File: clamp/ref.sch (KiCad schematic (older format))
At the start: 11 parts, among them P4 CONN_01X06, U12 LTZ1000, U13 LM741

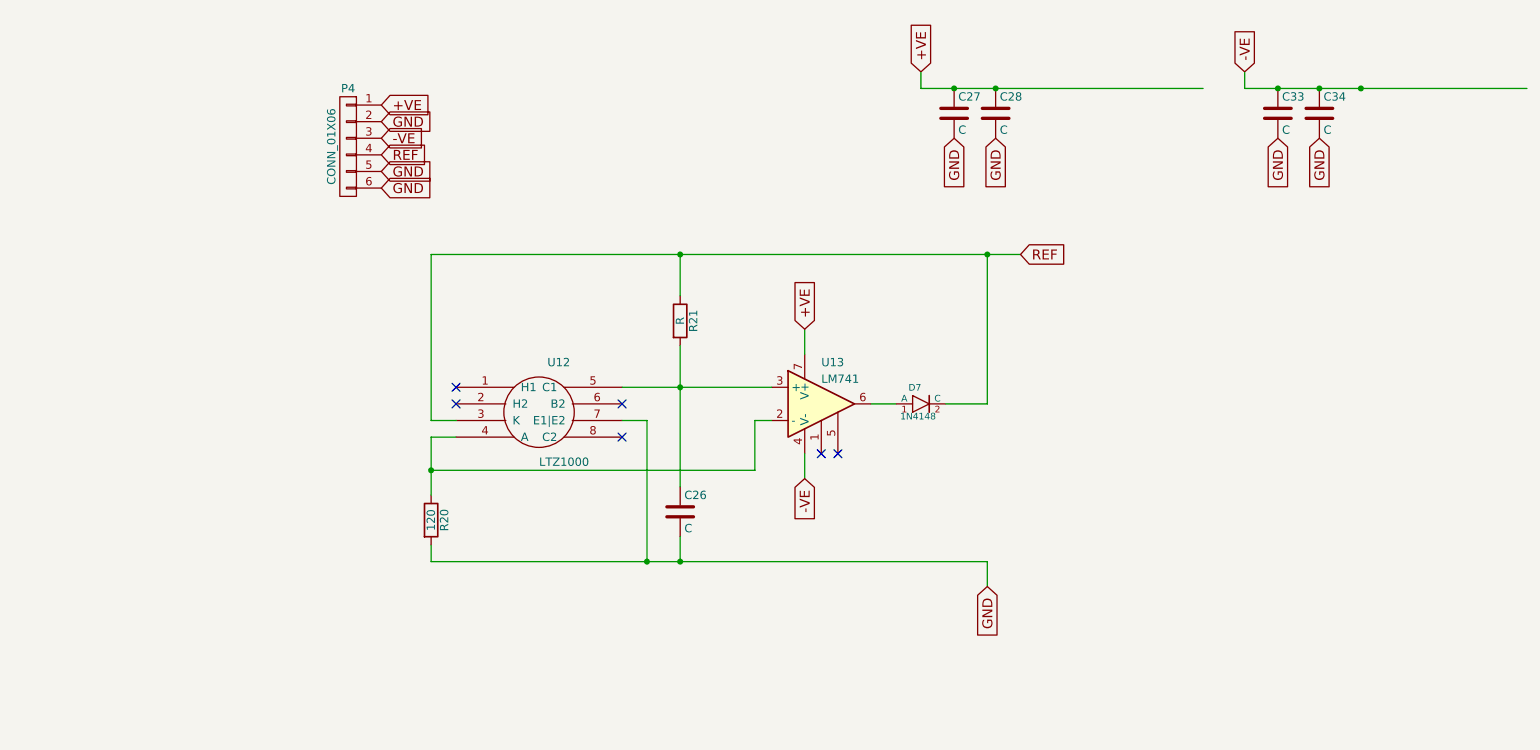
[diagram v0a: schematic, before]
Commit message: add heater feedback to ref
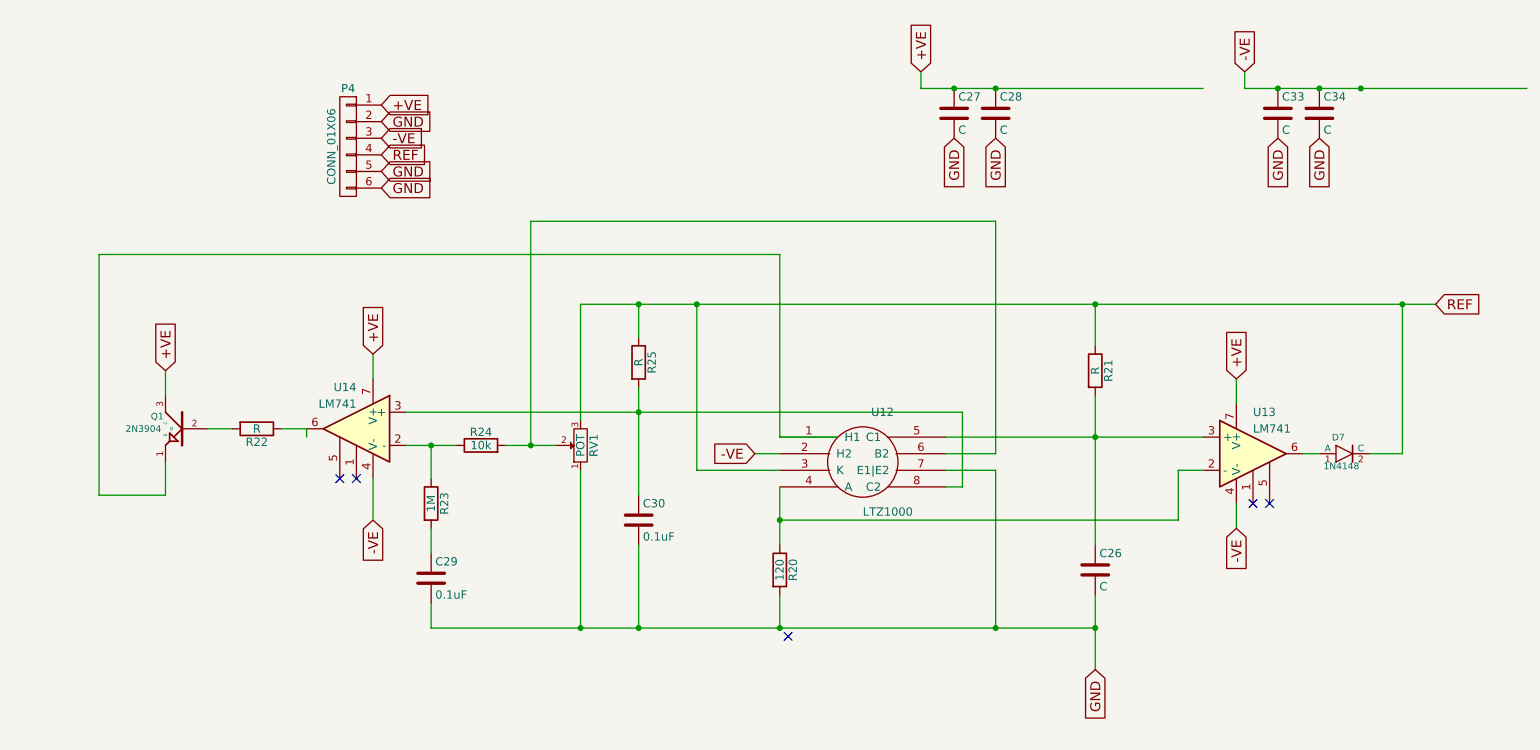
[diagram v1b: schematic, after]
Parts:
- added C29, C30: 0.1uF, symbol C
- added Q1: 2N3904, symbol 2N3904
- added R22, R25: R, symbol R
- added R23: 1M, symbol R
- added R24: 10k, symbol R
- added RV1: POT, symbol POT
- added U14: LM741, SMD_Packages:SOIC-8-N, symbol LM741
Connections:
- wire segments 26 -> 54
- no-connect marks 6 -> 5
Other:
- moved on the sheet: C26, D7, R20, R21, U12, U13

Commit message: tidy
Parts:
- C26: value C -> 22nF
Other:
- moved on the sheet: C29
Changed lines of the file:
@@
 	1    0    0    -1
 $EndComp
-Text GLabel 8250 2700 1    60   Input ~ 0
+Text GLabel 8250 2650 1    60   Input ~ 0
 +VE
 $Comp
@@
 Connection ~ 7400 3050
 Wire Wire Line
-	7900 3550 7900 3250
+	7900 3600 7900 3250
 Wire Wire Line
 	7900 3250 8050 3250
-Connection ~ 5500 3550
+Connection ~ 5500 3600
 Wire Wire Line
 	5500 4200 5500 4000
@@
 P 7400 3850
 F 0 "C26" H 7425 3950 50  0000 L CNN
-F 1 "C" H 7425 3750 50  0000 L CNN
+F 1 "22nF" H 7425 3750 50  0000 L CNN
 F 2 "Capacitors_SMD:C_1206" H 7438 3700 50  0001 C CNN
 F 3 "" H 7400 3850 50  0000 C CNN
@@
 Connection ~ 7400 4200
 Wire Wire Line
-	8250 2700 8250 2850
+	8250 2650 8250 2850
 Text GLabel 8250 3600 3    60   Input ~ 0
 -VE
@@
 	6350 850  6350 950
 Wire Wire Line
-	6350 950  8050 950
+	6350 950  6800 950
 Connection ~ 6550 950
 Text GLabel 6550 1250 3    60   Input ~ 0
@@
 	8300 850  8300 950
 Wire Wire Line
-	8300 950  10000 950
+	8300 950  8750 950
 Connection ~ 8500 950
 Text GLabel 8500 1250 3    60   Input ~ 0
@@
 Text GLabel 8750 1250 3    60   Input ~ 0
 GND
-Connection ~ 9000 950
 Text GLabel 8300 850  1    60   Input ~ 0
 -VE
@@
 L C C29
 U 1 1 5864BE17
-P 3400 3900
-F 0 "C29" H 3425 4000 50  0000 L CNN
-F 1 "0.1uF" H 3425 3800 50  0000 L CNN
-F 2 "" H 3438 3750 50  0000 C CNN
-F 3 "" H 3400 3900 50  0000 C CNN
-	1    3400 3900
-	1    0    0    -1
-$EndComp
-Wire Wire Line
-	3400 3600 3400 3750
-Wire Wire Line
-	3400 4050 3400 4200
+P 3400 3850
+F 0 "C29" H 3425 3950 50  0000 L CNN
+F 1 "0.1uF" H 3425 3750 50  0000 L CNN
+F 2 "" H 3438 3700 50  0000 C CNN
+F 3 "" H 3400 3850 50  0000 C CNN
+	1    3400 3850
+	1    0    0    -1
+$EndComp
+Wire Wire Line
+	3400 3600 3400 3700
+Wire Wire Line
+	3400 4000 3400 4200
 Connection ~ 4300 4200
 Wire Wire Line
@@
 	-1   0    0    -1
 $EndComp
-Text GLabel 1800 2650 1    60   Input ~ 0
-+VE
-Wire Wire Line
-	1800 2650 1800 2800
+Text GLabel 1800 2550 1    60   Input ~ 0
++VE
+Wire Wire Line
+	1800 2550 1800 2800
 $Comp
 L R R22
@@
 	3400 4200 7400 4200
 Wire Wire Line
-	5500 3550 7900 3550
+	5500 3600 7900 3600
 Wire Wire Line
 	8650 3150 8750 3150
 Text GLabel 3050 2550 1    60   Input ~ 0
 +VE
-Text GLabel 3050 3550 3    60   Input ~ 0
--VE
-Wire Wire Line
-	3050 3550 3050 3300
+Text GLabel 3050 3500 3    60   Input ~ 0
+-VE
+Wire Wire Line
+	3050 3500 3050 3300
 Wire Wire Line
 	3050 2550 3050 2700

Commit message: update
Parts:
- added D8: 1N4148, Diodes_SMD:MiniMELF_Standard, symbol 1N4148
- C29, C30: footprint (none) -> Capacitors_SMD:C_1206
- Q1: footprint (none) -> TO_SOT_Packages_SMD:SOT-23
- R21: renamed from R25; value R -> 70k
- R22: value R -> 1k; footprint (none) -> Resistors_SMD:R_1206
- R23, R24: footprint (none) -> Resistors_SMD:R_1206
- RV1: footprint (none) -> Potentiometers:Potentiometer_Bourns_3296Y_3-8Zoll_Angular_ScrewUp
- r1: renamed from R21; value R -> 70k
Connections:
- wire segments 54 -> 56
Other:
- moved on the sheet: r1
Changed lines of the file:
@@
 	9050 3150 9250 3150
 Wire Wire Line
-	9250 2250 9250 3150
-Wire Wire Line
-	5000 2250 5000 3250
-Wire Wire Line
-	5000 3250 5500 3250
+	9250 3150 9250 2250
+Wire Wire Line
+	5500 2250 5500 3250
 $Comp
 L R R20
@@
 	5500 3350 5500 3700
 $Comp
-L R R21
+L R r1
 U 1 1 5864309C
-P 7400 2650
-F 0 "R21" V 7480 2650 50  0000 C CNN
-F 1 "R" V 7400 2650 50  0000 C CNN
-F 2 "Resistors_ThroughHole:Resistor_TO-220_Vertical" V 7330 2650 50  0001 C CNN
-F 3 "" H 7400 2650 50  0000 C CNN
-	1    7400 2650
-	1    0    0    -1
-$EndComp
-Wire Wire Line
-	7400 2250 7400 2500
+P 7400 2600
+F 0 "r1" V 7480 2600 50  0000 C CNN
+F 1 "70k" V 7400 2600 50  0000 C CNN
+F 2 "Resistors_ThroughHole:Resistor_TO-220_Vertical" V 7330 2600 50  0001 C CNN
+F 3 "" H 7400 2600 50  0000 C CNN
+	1    7400 2600
+	1    0    0    -1
+$EndComp
+Wire Wire Line
+	7400 2250 7400 2450
 Connection ~ 7400 2250
 Wire Wire Line
-	7400 2800 7400 3700
+	7400 2750 7400 3700
 Wire Wire Line
 	6500 3250 6800 3250
 Wire Wire Line
-	6800 4200 6800 3250
+	6800 3250 6800 4200
 Connection ~ 6800 4200
 Connection ~ 7400 3050
@@
 Text GLabel 8300 850  1    60   Input ~ 0
 -VE
-$Comp
-L R R25
-U 1 1 58649A40
-P 4650 2600
-F 0 "R25" V 4730 2600 50  0000 C CNN
-F 1 "R" V 4650 2600 50  0000 C CNN
-F 2 "" V 4580 2600 50  0000 C CNN
-F 3 "" H 4650 2600 50  0000 C CNN
-	1    4650 2600
-	1    0    0    -1
-$EndComp
 Wire Wire Line
 	4650 2250 4650 2450
@@
 F 0 "C30" H 4675 3650 50  0000 L CNN
 F 1 "0.1uF" H 4675 3450 50  0000 L CNN
-F 2 "" H 4688 3400 50  0000 C CNN
+F 2 "Capacitors_SMD:C_1206" H 4688 3400 50  0001 C CNN
 F 3 "" H 4650 3550 50  0000 C CNN
 	1    4650 3550
@@
 F 0 "RV1" H 4300 3020 50  0000 C CNN
 F 1 "POT" H 4300 3100 50  0000 C CNN
-F 2 "" H 4300 3100 50  0000 C CNN
+F 2 "Potentiometers:Potentiometer_Bourns_3296Y_3-8Zoll_Angular_ScrewUp" H 4300 3100 50  0001 C CNN
 F 3 "" H 4300 3100 50  0000 C CNN
 	1    4300 3100
 	0    -1   -1   0
 $EndComp
-Connection ~ 5000 2250
+Connection ~ 5500 2250
 Wire Wire Line
 	3250 2900 6600 2900
@@
 F 0 "R24" V 3780 3100 50  0000 C CNN
 F 1 "10k" V 3700 3100 50  0000 C CNN
-F 2 "" V 3630 3100 50  0000 C CNN
+F 2 "Resistors_SMD:R_1206" V 3630 3100 50  0001 C CNN
 F 3 "" H 3700 3100 50  0000 C CNN
 	1    3700 3100
@@
 Wire Wire Line
 	3850 3100 4150 3100
-Text GLabel 5350 3150 0    60   Input ~ 0
--VE
-Wire Wire Line
-	5350 3150 5500 3150
+Text GLabel 5050 4500 3    60   Input ~ 0
+-VE
+Wire Wire Line
+	5050 3150 5500 3150
 $Comp
 L R R23
@@
 F 0 "R23" V 3480 3450 50  0000 C CNN
 F 1 "1M" V 3400 3450 50  0000 C CNN
-F 2 "" V 3330 3450 50  0000 C CNN
+F 2 "Resistors_SMD:R_1206" V 3330 3450 50  0001 C CNN
 F 3 "" H 3400 3450 50  0000 C CNN
 	1    3400 3450
@@
 F 0 "C29" H 3425 3950 50  0000 L CNN
 F 1 "0.1uF" H 3425 3750 50  0000 L CNN
-F 2 "" H 3438 3700 50  0000 C CNN
+F 2 "Capacitors_SMD:C_1206" H 3438 3700 50  0001 C CNN
 F 3 "" H 3400 3850 50  0000 C CNN
 	1    3400 3850
@@
 Wire Wire Line
 	3400 4000 3400 4200
-Connection ~ 4300 4200
 Wire Wire Line
 	3400 3100 3400 3300
@@
 F 0 "Q1" H 2050 3075 40  0000 C CNN
 F 1 "2N3904" H 2025 3000 40  0000 L CNN
-F 2 "" H 1900 3000 60  0001 C CNN
+F 2 "TO_SOT_Packages_SMD:SOT-23" H 1900 3000 60  0001 C CNN
 F 3 "" H 1900 3000 60  0001 C CNN
 	1    1900 3000
@@
 P 2350 3000
 F 0 "R22" V 2430 3000 50  0000 C CNN
-F 1 "R" V 2350 3000 50  0000 C CNN
-F 2 "" V 2280 3000 50  0000 C CNN
+F 1 "1k" V 2350 3000 50  0000 C CNN
+F 2 "Resistors_SMD:R_1206" V 2280 3000 50  0001 C CNN
 F 3 "" H 2350 3000 50  0000 C CNN
 	1    2350 3000
@@
 	1400 3400 1800 3400
 Wire Wire Line
-	1400 3400 1400 1950
-Wire Wire Line
-	1400 1950 5500 1950
-Wire Wire Line
-	5500 3050 5850 3050
-Wire Wire Line
-	5500 1950 5500 3050
+	1400 1950 1400 4200
+Wire Wire Line
+	1400 1950 5050 1950
+Wire Wire Line
+	5050 1950 5050 3050
 Wire Wire Line
 	4300 2250 9450 2250
 Wire Wire Line
-	3400 4200 7400 4200
+	4300 4200 7400 4200
 Wire Wire Line
 	5500 3600 7900 3600
@@
 	6800 3150 6500 3150
 Wire Wire Line
-	6800 1750 6800 3150
-Wire Wire Line
-	4000 1750 4000 3100
+	6800 2100 6800 3150
+Wire Wire Line
+	4000 2100 4000 3100
 Connection ~ 4000 3100
 Wire Wire Line
-	6800 1750 4000 1750
+	6800 2100 4000 2100
+Wire Wire Line
+	1400 4200 3400 4200
+Connection ~ 1400 3400
+$Comp
+L 1N4148 D8
+U 1 1 5864EF9B
+P 5050 3800
+F 0 "D8" H 4975 3875 40  0000 L BNN
+F 1 "1N4148" H 4925 3725 40  0000 L CNN
+F 2 "Diodes_SMD:MiniMELF_Standard" H 5050 3950 30  0001 C CNN
+F 3 "" H 5050 3800 60  0000 C CNN
+	1    5050 3800
+	0    1    1    0
+$EndComp
+Wire Wire Line
+	5050 3150 5050 3650
+Wire Wire Line
+	5050 3950 5050 4500
+Wire Wire Line
+	5050 3050 5500 3050
+$Comp
+L R R21
+U 1 1 58649A40
+P 4650 2600
+F 0 "R21" V 4730 2600 50  0000 C CNN
+F 1 "70k" V 4650 2600 50  0000 C CNN
+F 2 "" V 4580 2600 50  0001 C CNN
+F 3 "" H 4650 2600 50  0000 C CNN
+	1    4650 2600
+	1    0    0    -1
+$EndComp
 $EndSCHEMATC
